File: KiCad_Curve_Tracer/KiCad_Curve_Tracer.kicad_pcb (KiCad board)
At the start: 2 copper layers, 20.3 x 31.7 mm, 11 parts, among them J1 Vi, J2 DUT, J3 rng, J4 Input, J5 Vo, U1 Opamp_Dual

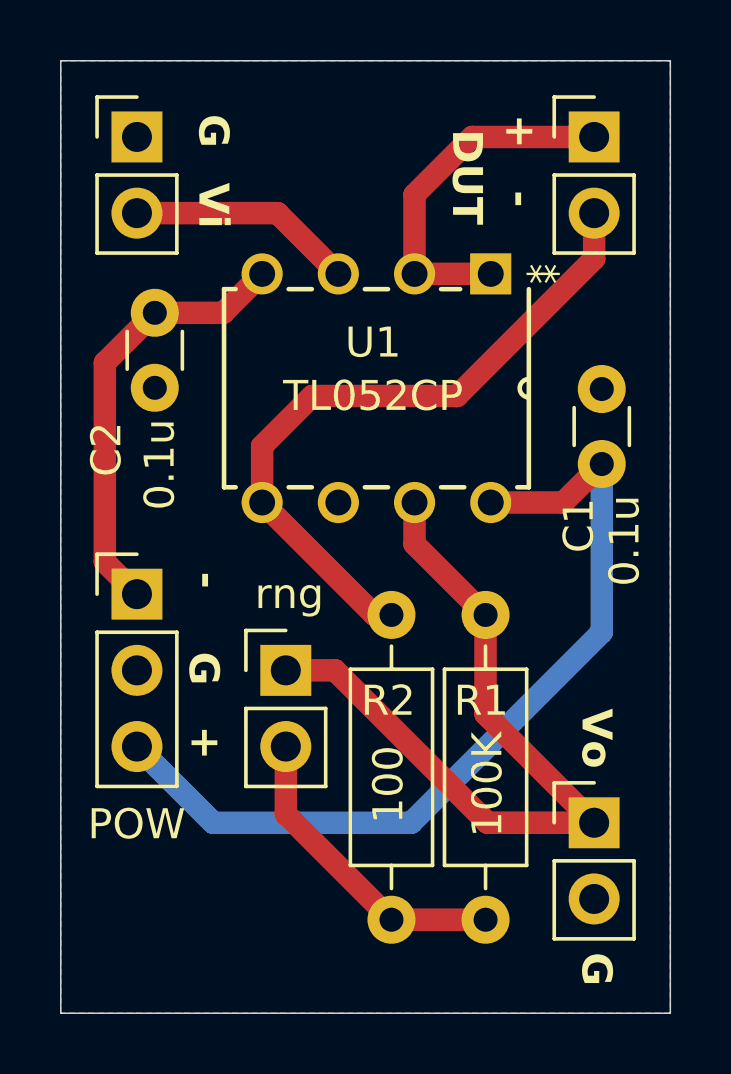
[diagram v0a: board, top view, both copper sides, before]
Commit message: Fixed the curve tracer PCB
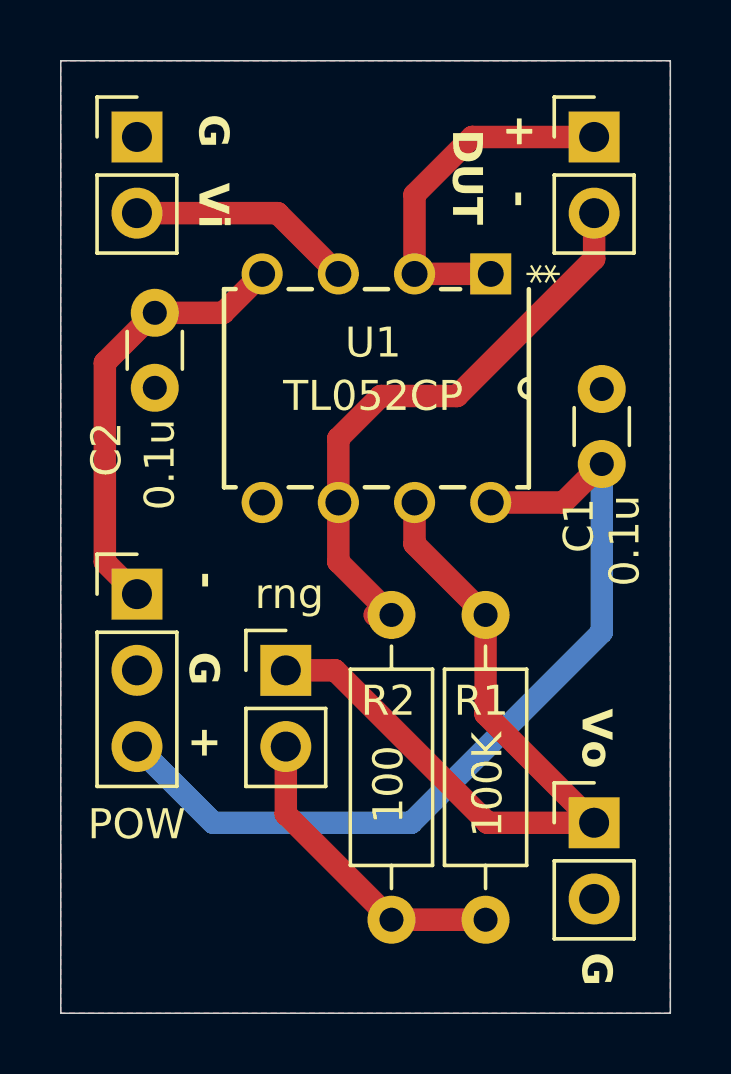
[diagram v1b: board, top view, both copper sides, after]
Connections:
- U1 pad 5: /opamp curve tracer/DUT- -> GND
- U1 pad 6: GND -> /opamp curve tracer/DUT-
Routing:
- net /opamp curve tracer/DUT-: track 22.9 -> 19.7 mm
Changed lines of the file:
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@@
 			(drillshape 0)
 			(scaleselection 1)
-			(outputdirectory "Fab files/")
+			(outputdirectory "fab files/")
 		)
 	)
@@
 			(layers "*.Cu" "*.Mask")
 			(remove_unused_layers no)
-			(net 5 "/opamp curve tracer/DUT-")
+			(net 1 "GND")
 			(pinfunction "+")
 			(pintype "input")
@@
 			(layers "*.Cu" "*.Mask")
 			(remove_unused_layers no)
-			(net 1 "GND")
+			(net 5 "/opamp curve tracer/DUT-")
 			(pinfunction "-")
 			(pintype "input")
@@
 	)
 	(segment
-		(start 53.641158 51.493113)
-		(end 49.893415 47.74537)
+		(start 60.96 38.1)
+		(end 60.96 39.624)
 		(width 0.75)
 		(layer "F.Cu")
@@
 	)
 	(segment
-		(start 51.562 44.196)
-		(end 49.893415 45.864585)
+		(start 53.848 44.196)
+		(end 52.433415 45.610585)
 		(width 0.75)
 		(layer "F.Cu")
@@
 	)
 	(segment
-		(start 54.204239 51.493113)
-		(end 53.641158 51.493113)
+		(start 52.433415 45.610585)
+		(end 52.433415 47.74537)
 		(width 0.75)
 		(layer "F.Cu")
@@
 	)
 	(segment
-		(start 49.893415 45.864585)
-		(end 49.893415 47.74537)
+		(start 60.96 39.624)
+		(end 56.388 44.196)
 		(width 0.75)
 		(layer "F.Cu")
@@
 	)
 	(segment
-		(start 60.96 39.624)
-		(end 56.388 44.196)
+		(start 54.204239 51.493113)
+		(end 53.641158 51.493113)
 		(width 0.75)
 		(layer "F.Cu")
@@
 	)
 	(segment
-		(start 60.96 38.1)
-		(end 60.96 39.624)
+		(start 52.433415 49.722289)
+		(end 54.204239 51.493113)
 		(width 0.75)
 		(layer "F.Cu")
@@
 	(segment
 		(start 56.388 44.196)
-		(end 51.562 44.196)
+		(end 53.848 44.196)
+		(width 0.75)
+		(layer "F.Cu")
+		(net 5)
+	)
+	(segment
+		(start 52.433415 47.74537)
+		(end 52.433415 49.722289)
 		(width 0.75)
 		(layer "F.Cu")
